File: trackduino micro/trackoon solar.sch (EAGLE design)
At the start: 62 parts, among them IC1 MCP73871, IC2 74AHC1G125DBV, SW1 SPST_TACT-KMR2, U1 ATMEGA168MLF, Y1 16MHZ

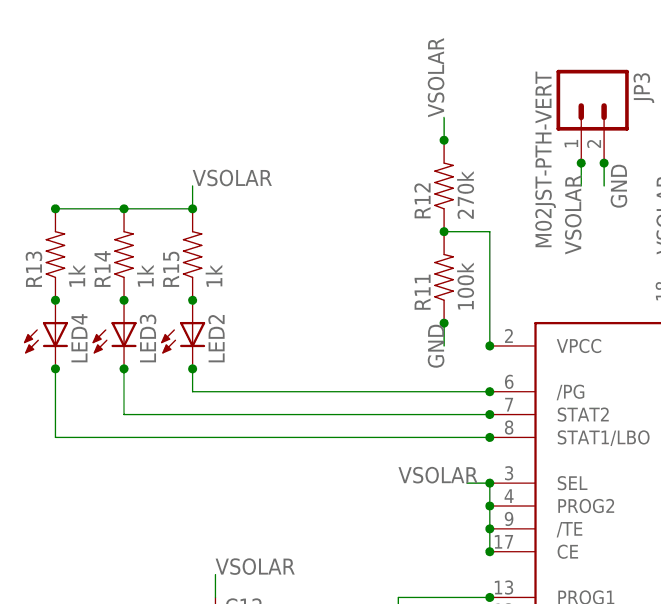
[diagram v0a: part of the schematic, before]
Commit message: solar board routing
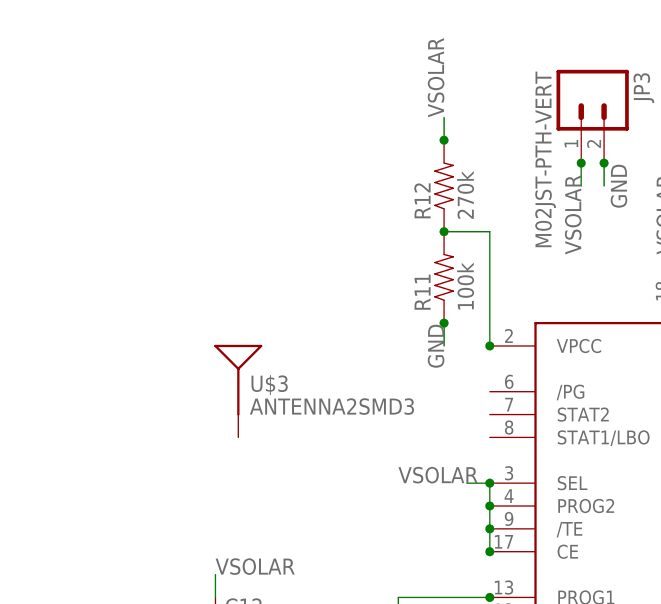
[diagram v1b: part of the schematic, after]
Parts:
- removed LED2, LED3, LED4: (no value), adafruit:LEDCHIPLED_0805
- removed R13, R14, R15: 1k, SparkFun-Resistors:RESISTOR0805-RES
- added U$3: ANTENNA2SMD3, SparkFun-RF:ANTENNA2SMD3
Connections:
- removed net N$19: LED2.A, R15.1
- removed net N$20: LED3.A, R14.1
- removed net N$21: LED4.A, R13.1
- removed net N$22: IC1./PG, LED2.C
- removed net STAT1: IC1.STAT1/LBO, LED4.C
- removed net STAT2: IC1.STAT2, LED3.C
- net VSOLAR: no longer R13.2, R14.2, R15.2
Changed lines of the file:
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@@
 <part name="R11" library="SparkFun-Resistors" deviceset="RESISTOR" device="0805-RES" value="100k"/>
 <part name="R12" library="SparkFun-Resistors" deviceset="RESISTOR" device="0805-RES" value="270k"/>
-<part name="R13" library="SparkFun-Resistors" deviceset="RESISTOR" device="0805-RES" value="1k"/>
-<part name="R14" library="SparkFun-Resistors" deviceset="RESISTOR" device="0805-RES" value="1k"/>
-<part name="R15" library="SparkFun-Resistors" deviceset="RESISTOR" device="0805-RES" value="1k"/>
-<part name="LED2" library="adafruit" deviceset="LED" device="CHIPLED_0805"/>
-<part name="LED3" library="adafruit" deviceset="LED" device="CHIPLED_0805"/>
-<part name="LED4" library="adafruit" deviceset="LED" device="CHIPLED_0805"/>
 <part name="R16" library="SparkFun-Resistors" deviceset="RESISTOR" device="0805-RES" value="2k"/>
 <part name="R17" library="SparkFun-Resistors" deviceset="RESISTOR" device="0805-RES" value="100k"/>
@@
 <part name="JP3" library="SparkFun-Connectors" deviceset="M02" device="JST-PTH-VERT" value="M02JST-PTH-VERT"/>
 <part name="C12" library="adafruit" deviceset="CPOL-US" device="153CLV-1012"/>
+<part name="U$3" library="SparkFun-RF" deviceset="ANTENNA2" device="SMD3"/>
 </parts>
 <sheets>
@@
 <instance part="R11" gate="G$1" x="-66.04" y="114.3" rot="R90"/>
 <instance part="R12" gate="G$1" x="-66.04" y="124.46" rot="R90"/>
-<instance part="R13" gate="G$1" x="-109.22" y="116.84" rot="R90"/>
-<instance part="R14" gate="G$1" x="-101.6" y="116.84" rot="R90"/>
-<instance part="R15" gate="G$1" x="-93.98" y="116.84" rot="R90"/>
-<instance part="LED2" gate="G$1" x="-93.98" y="109.22"/>
-<instance part="LED3" gate="G$1" x="-101.6" y="109.22"/>
-<instance part="LED4" gate="G$1" x="-109.22" y="109.22"/>
 <instance part="R16" gate="G$1" x="-71.12" y="71.12" rot="R90"/>
 <instance part="R17" gate="G$1" x="-63.5" y="71.12" rot="R90"/>
@@
 <instance part="JP3" gate="G$1" x="-50.8" y="134.62" rot="R270"/>
 <instance part="C12" gate="G$1" x="-91.44" y="76.2"/>
+<instance part="U$3" gate="G$1" x="-88.9" y="101.6"/>
 </instances>
 <busses>
@@
 </segment>
 </net>
-<net name="N$19" class="0">
-<segment>
-<pinref part="R15" gate="G$1" pin="1"/>
-<pinref part="LED2" gate="G$1" pin="A"/>
-<junction x="-93.98" y="111.76"/>
-</segment>
-</net>
-<net name="N$20" class="0">
-<segment>
-<pinref part="R14" gate="G$1" pin="1"/>
-<pinref part="LED3" gate="G$1" pin="A"/>
-<junction x="-101.6" y="111.76"/>
-</segment>
-</net>
-<net name="N$21" class="0">
-<segment>
-<pinref part="R13" gate="G$1" pin="1"/>
-<pinref part="LED4" gate="G$1" pin="A"/>
-<junction x="-109.22" y="111.76"/>
-</segment>
-</net>
 <net name="VSOLAR" class="0">
 <segment>
@@
 <label x="-66.04" y="132.08" size="1.778" layer="95" rot="R90"/>
 <junction x="-66.04" y="129.54"/>
-</segment>
-<segment>
-<pinref part="R13" gate="G$1" pin="2"/>
-<pinref part="R15" gate="G$1" pin="2"/>
-<wire x1="-109.22" y1="121.92" x2="-101.6" y2="121.92" width="0.1524" layer="91"/>
-<wire x1="-101.6" y1="121.92" x2="-93.98" y2="121.92" width="0.1524" layer="91"/>
-<wire x1="-93.98" y1="121.92" x2="-93.98" y2="124.46" width="0.1524" layer="91"/>
-<label x="-93.98" y="124.46" size="1.778" layer="95"/>
-<junction x="-93.98" y="121.92"/>
-<pinref part="R14" gate="G$1" pin="2"/>
-<junction x="-101.6" y="121.92"/>
-<junction x="-109.22" y="121.92"/>
 </segment>
 <segment>
@@
 </segment>
 </net>
-<net name="N$22" class="0">
-<segment>
-<pinref part="LED2" gate="G$1" pin="C"/>
-<wire x1="-93.98" y1="104.14" x2="-93.98" y2="101.6" width="0.1524" layer="91"/>
-<pinref part="IC1" gate="G$1" pin="/PG"/>
-<wire x1="-93.98" y1="101.6" x2="-60.96" y2="101.6" width="0.1524" layer="91"/>
-<junction x="-60.96" y="101.6"/>
-<junction x="-93.98" y="104.14"/>
-</segment>
-</net>
-<net name="STAT2" class="0">
-<segment>
-<pinref part="IC1" gate="G$1" pin="STAT2"/>
-<pinref part="LED3" gate="G$1" pin="C"/>
-<wire x1="-60.96" y1="99.06" x2="-101.6" y2="99.06" width="0.1524" layer="91"/>
-<wire x1="-101.6" y1="99.06" x2="-101.6" y2="104.14" width="0.1524" layer="91"/>
-<junction x="-60.96" y="99.06"/>
-<junction x="-101.6" y="104.14"/>
-</segment>
-</net>
-<net name="STAT1" class="0">
-<segment>
-<pinref part="IC1" gate="G$1" pin="STAT1/LBO"/>
-<pinref part="LED4" gate="G$1" pin="C"/>
-<wire x1="-60.96" y1="96.52" x2="-109.22" y2="96.52" width="0.1524" layer="91"/>
-<wire x1="-109.22" y1="96.52" x2="-109.22" y2="104.14" width="0.1524" layer="91"/>
-<junction x="-60.96" y="96.52"/>
-<junction x="-109.22" y="104.14"/>
-</segment>
-</net>

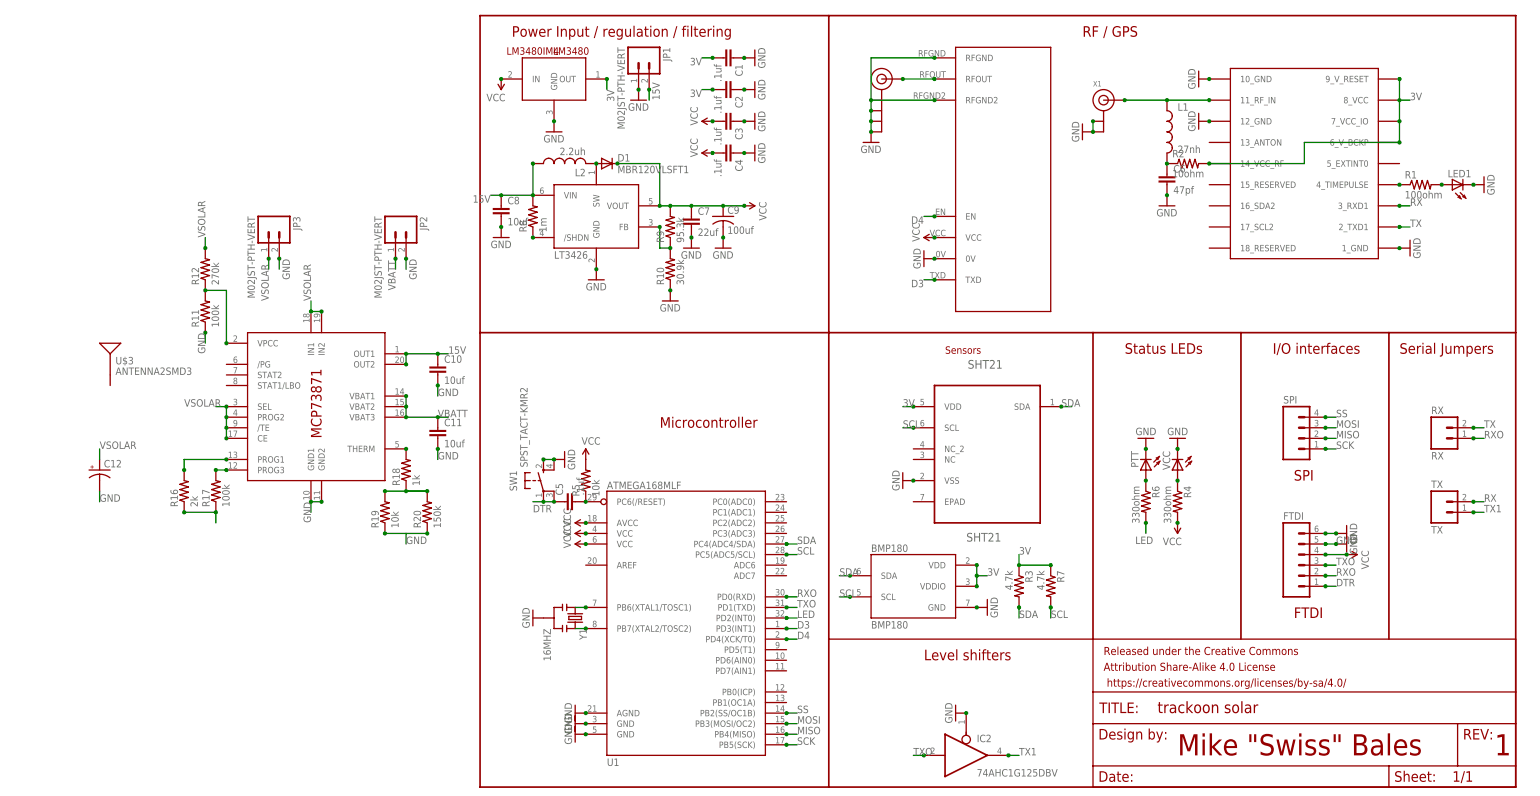
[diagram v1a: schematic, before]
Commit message: solar replace antenna
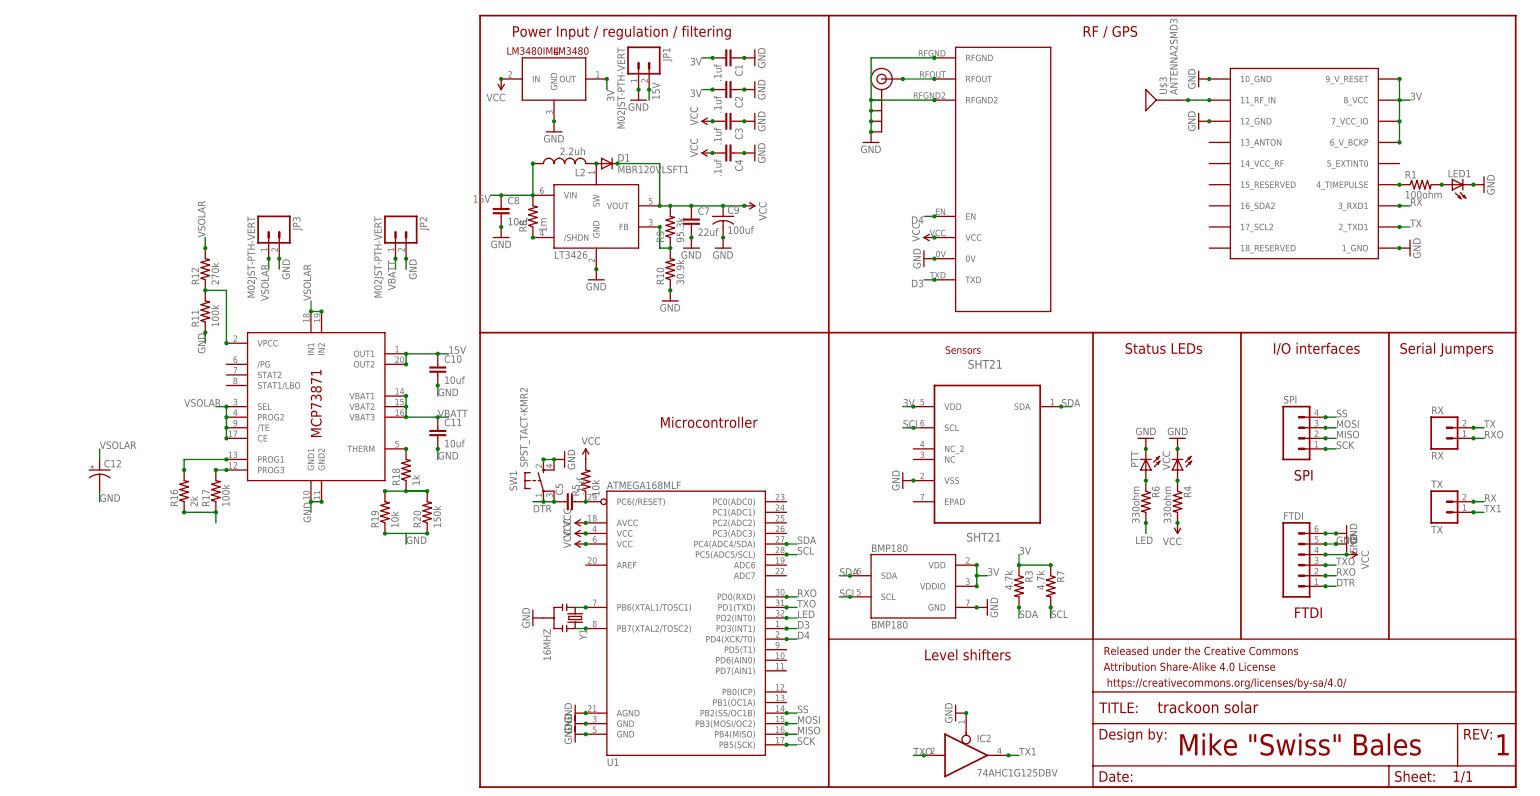
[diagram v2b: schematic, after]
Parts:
- removed C6: 47pf, SparkFun-Capacitors:CAP0805
- removed L1: 27nh, SparkFun-Passives:INDUCTOR0805
- removed R2: 10ohm, SparkFun-Resistors:RESISTOR0805-RES
- removed X1: (no value), adafruit:ANTENNA_U.FL
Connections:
- removed net N$24: C6.1, L1.2, R2.1
- net 3V: no longer R2.2, U$1.14_VCC_RF
- net GND: no longer C6.2, X1.GND@0, X1.GND@1
- net N$6: now also U$3.SIGNAL; no longer L1.1, X1.SIGNAL
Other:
- moved on the sheet: U$3
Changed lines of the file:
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@@
 <part name="GND8" library="SparkFun-Aesthetics" deviceset="GND" device=""/>
 <part name="GND9" library="SparkFun-Aesthetics" deviceset="GND" device=""/>
-<part name="GND11" library="SparkFun-Aesthetics" deviceset="GND" device=""/>
 <part name="GND13" library="SparkFun-Aesthetics" deviceset="GND" device=""/>
 <part name="GND14" library="SparkFun-Aesthetics" deviceset="GND" device=""/>
@@
 <part name="Y1" library="SparkFun-FreqCtrl" deviceset="RESONATOR" device="16MHZ" value="16MHZ"/>
 <part name="U$1" library="Ava" deviceset="UBLOX_MAX" device=""/>
-<part name="X1" library="adafruit" deviceset="ANTENNA_U.FL" device=""/>
 <part name="SW1" library="adafruit" deviceset="SPST_TACT" device="-KMR2"/>
 <part name="GND1" library="SparkFun-Aesthetics" deviceset="GND" device=""/>
 <part name="GND3" library="SparkFun-Aesthetics" deviceset="GND" device=""/>
-<part name="L1" library="SparkFun-Passives" deviceset="INDUCTOR" device="0805" value="27nh"/>
-<part name="R2" library="SparkFun-Resistors" deviceset="RESISTOR" device="0805-RES" value="10ohm"/>
-<part name="C6" library="SparkFun-Capacitors" deviceset="CAP" device="0805" value="47pf"/>
-<part name="GND6" library="SparkFun-Aesthetics" deviceset="GND" device=""/>
 <part name="RX" library="SparkFun-Connectors" deviceset="M02" device="PTH" value="RX"/>
 <part name="GND10" library="SparkFun-Aesthetics" deviceset="GND" device=""/>
@@
 <instance part="GND8" gate="1" x="241.3" y="144.78" rot="R90"/>
 <instance part="GND9" gate="1" x="223.52" y="129.54" rot="R90"/>
-<instance part="GND11" gate="1" x="144.78" y="157.48" rot="R270"/>
 <instance part="GND13" gate="1" x="172.72" y="160.02" rot="R270"/>
 <instance part="GND14" gate="1" x="172.72" y="170.18" rot="R270"/>
@@
 <instance part="Y1" gate="G$1" x="22.86" y="40.64" rot="R270"/>
 <instance part="U$1" gate="G$1" x="198.12" y="154.94"/>
-<instance part="X1" gate="G$1" x="149.86" y="165.1"/>
 <instance part="SW1" gate="G$1" x="15.24" y="73.66"/>
 <instance part="GND1" gate="1" x="66.04" y="167.64" rot="R90"/>
 <instance part="GND3" gate="1" x="17.78" y="157.48"/>
-<instance part="L1" gate="G$1" x="165.1" y="157.48"/>
-<instance part="R2" gate="G$1" x="170.18" y="149.86"/>
-<instance part="C6" gate="G$1" x="165.1" y="144.78"/>
-<instance part="GND6" gate="1" x="165.1" y="139.7"/>
 <instance part="RX" gate="G$1" x="231.14" y="83.82"/>
 <instance part="GND10" gate="1" x="208.28" y="58.42" rot="R90"/>
@@
 <instance part="JP3" gate="G$1" x="-50.8" y="134.62" rot="R270"/>
 <instance part="C12" gate="G$1" x="-91.44" y="76.2"/>
-<instance part="U$3" gate="G$1" x="-88.9" y="101.6"/>
+<instance part="U$3" gate="G$1" x="165.1" y="165.1" rot="R90"/>
 </instances>
 <busses>
@@
 </segment>
 <segment>
-<pinref part="GND11" gate="1" pin="GND"/>
-<pinref part="X1" gate="G$1" pin="GND@0"/>
-<pinref part="X1" gate="G$1" pin="GND@1"/>
-<wire x1="147.32" y1="157.48" x2="147.32" y2="160.02" width="0.1524" layer="91"/>
-<junction x="147.32" y="157.48"/>
-<junction x="147.32" y="160.02"/>
-</segment>
-<segment>
 <pinref part="C1" gate="G$1" pin="1"/>
 <pinref part="GND15" gate="1" pin="GND"/>
@@
 <pinref part="GND3" gate="1" pin="GND"/>
 <junction x="17.78" y="160.02"/>
-</segment>
-<segment>
-<pinref part="C6" gate="G$1" pin="2"/>
-<pinref part="GND6" gate="1" pin="GND"/>
-<junction x="165.1" y="142.24"/>
 </segment>
 <segment>
@@
 <pinref part="U$1" gate="G$1" pin="6_V_BCKP"/>
 <wire x1="220.98" y1="160.02" x2="220.98" y2="154.94" width="0.1524" layer="91"/>
-<wire x1="220.98" y1="154.94" x2="198.12" y2="154.94" width="0.1524" layer="91"/>
-<wire x1="198.12" y1="154.94" x2="198.12" y2="149.86" width="0.1524" layer="91"/>
-<pinref part="U$1" gate="G$1" pin="14_VCC_RF"/>
-<wire x1="198.12" y1="149.86" x2="175.26" y2="149.86" width="0.1524" layer="91"/>
-<pinref part="R2" gate="G$1" pin="2"/>
-<junction x="175.26" y="149.86"/>
 <junction x="220.98" y="154.94"/>
 </segment>
@@
 </segment>
 </net>
-<net name="N$6" class="0">
-<segment>
-<wire x1="175.26" y1="165.1" x2="165.1" y2="165.1" width="0.1524" layer="91"/>
-<pinref part="U$1" gate="G$1" pin="11_RF_IN"/>
-<pinref part="X1" gate="G$1" pin="SIGNAL"/>
-<junction x="154.94" y="165.1"/>
-<junction x="175.26" y="165.1"/>
-<pinref part="L1" gate="G$1" pin="1"/>
-<wire x1="165.1" y1="165.1" x2="154.94" y2="165.1" width="0.1524" layer="91"/>
-<junction x="165.1" y="165.1"/>
-</segment>
-</net>
 <net name="RX" class="0">
 <segment>
@@
 <pinref part="R1" gate="G$1" pin="1"/>
 <junction x="220.98" y="144.78"/>
-</segment>
-</net>
-<net name="N$24" class="0">
-<segment>
-<pinref part="R2" gate="G$1" pin="1"/>
-<pinref part="L1" gate="G$1" pin="2"/>
-<pinref part="C6" gate="G$1" pin="1"/>
-<junction x="165.1" y="149.86"/>
-<pinref part="C6" gate="G$1" pin="1"/>
 </segment>
 </net>
@@
 </segment>
 </net>
+<net name="N$6" class="0">
+<segment>
+<pinref part="U$1" gate="G$1" pin="11_RF_IN"/>
+<pinref part="U$3" gate="G$1" pin="SIGNAL"/>
+<wire x1="170.18" y1="165.1" x2="175.26" y2="165.1" width="0.1524" layer="91"/>
+<junction x="170.18" y="165.1"/>
+<junction x="175.26" y="165.1"/>
+</segment>
+</net>
